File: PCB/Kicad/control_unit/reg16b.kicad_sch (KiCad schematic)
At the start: 2 parts, among them U6 74LS377, U7 74LS377

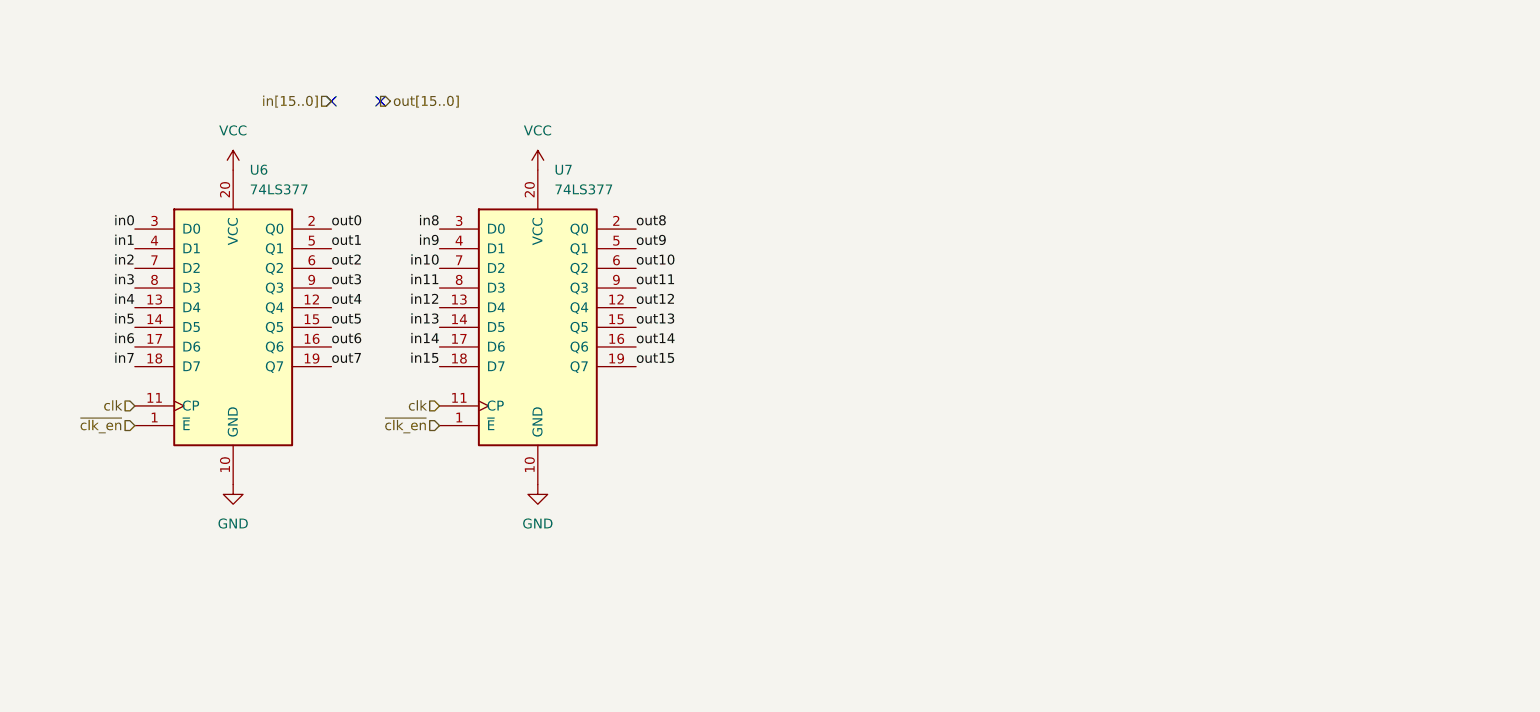
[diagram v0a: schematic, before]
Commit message: control unit schematic
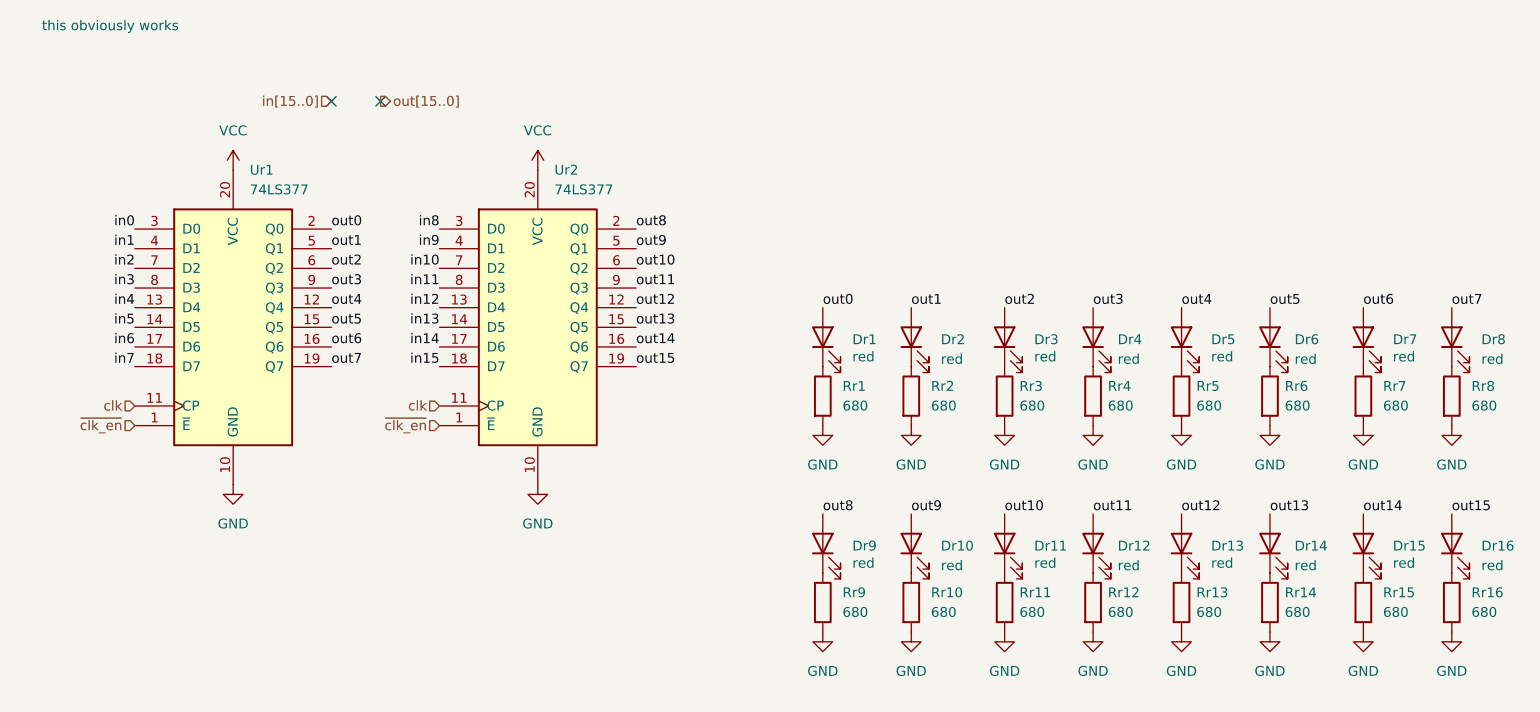
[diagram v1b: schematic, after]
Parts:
- added Dr1, Dr10, Dr11, Dr12, Dr13, Dr14, Dr15, Dr16, Dr2, Dr3, Dr4, Dr5, Dr6, Dr7, Dr8, Dr9: red, LED_SMD:LED_0603_1608Metric, symbol Device:LED
- added Rr1, Rr10, Rr11, Rr12, Rr13, Rr14, Rr15, Rr16, Rr2, Rr3, Rr4, Rr5, Rr6, Rr7, Rr8, Rr9: 680, Resistor_SMD:R_0402_1005Metric, symbol Device:R
- Ur1: renamed from U6; footprint (none) -> Package_SO:SSOP-20_5.3x7.2mm_P0.65mm
- Ur2: renamed from U7; footprint (none) -> Package_SO:SSOP-20_5.3x7.2mm_P0.65mm
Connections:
- net GND: now also Rr1.2, Rr10.2, Rr11.2, Rr12.2, Rr13.2, Rr14.2, Rr15.2, Rr16.2, Rr2.2, Rr3.2, Rr4.2, Rr5.2, Rr6.2, Rr7.2, Rr8.2, Rr9.2
- net out0: now also Dr1.2 (A)
- net out1: now also Dr2.2 (A)
- net out10: now also Dr11.2 (A)
- net out11: now also Dr12.2 (A)
- net out12: now also Dr13.2 (A)
- net out13: now also Dr14.2 (A)
- net out14: now also Dr15.2 (A)
- net out15: now also Dr16.2 (A)
- net out2: now also Dr3.2 (A)
- net out3: now also Dr4.2 (A)
- net out4: now also Dr5.2 (A)
- net out5: now also Dr6.2 (A)
- net out6: now also Dr7.2 (A)
- net out7: now also Dr8.2 (A)
- net out8: now also Dr9.2 (A)
- net out9: now also Dr10.2 (A)
- new net: Dr11.1 (K), Rr11.1
- new net: Dr3.1 (K), Rr3.1
- new net: Dr13.1 (K), Rr13.1
- new net: Dr7.1 (K), Rr7.1
- new net: Dr16.1 (K), Rr16.1
- new net: Dr14.1 (K), Rr14.1
- new net: Dr12.1 (K), Rr12.1
- new net: Dr6.1 (K), Rr6.1
- new net: Dr4.1 (K), Rr4.1
- new net: Dr1.1 (K), Rr1.1
- new net: Dr8.1 (K), Rr8.1
- new net: Dr5.1 (K), Rr5.1
- new net: Dr9.1 (K), Rr9.1
- new net: Dr15.1 (K), Rr15.1
- new net: Dr2.1 (K), Rr2.1
- new net: Dr10.1 (K), Rr10.1
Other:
- note added: "this obviously works"
- company: (none) -> AGH Logic Unit
- title: (none) -> 16bit Register

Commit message: control unit update
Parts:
- added Cinsr2, Cr2: 100nF, Capacitor_SMD:C_0402_1005Metric, symbol Device:C
- Ur1, Ur2: value 74LS377 -> 74377
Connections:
- net GND: now also Cinsr2.2, Cr2.2
- net VCC: now also Cinsr2.1, Cr2.1
